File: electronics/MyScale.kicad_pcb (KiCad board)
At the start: 2 copper layers, 74 x 50 mm, 50 parts, among them J1 Conn_01x03, J2 Conn_01x03, J3 Conn_01x03, J4 Conn_01x03, J5 Conn_01x02_MountingPin, J6 12402012E212A, J7 Conn_01x03, Q1 DMG2305UX, Q4 PNP, SW1 SW_Push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

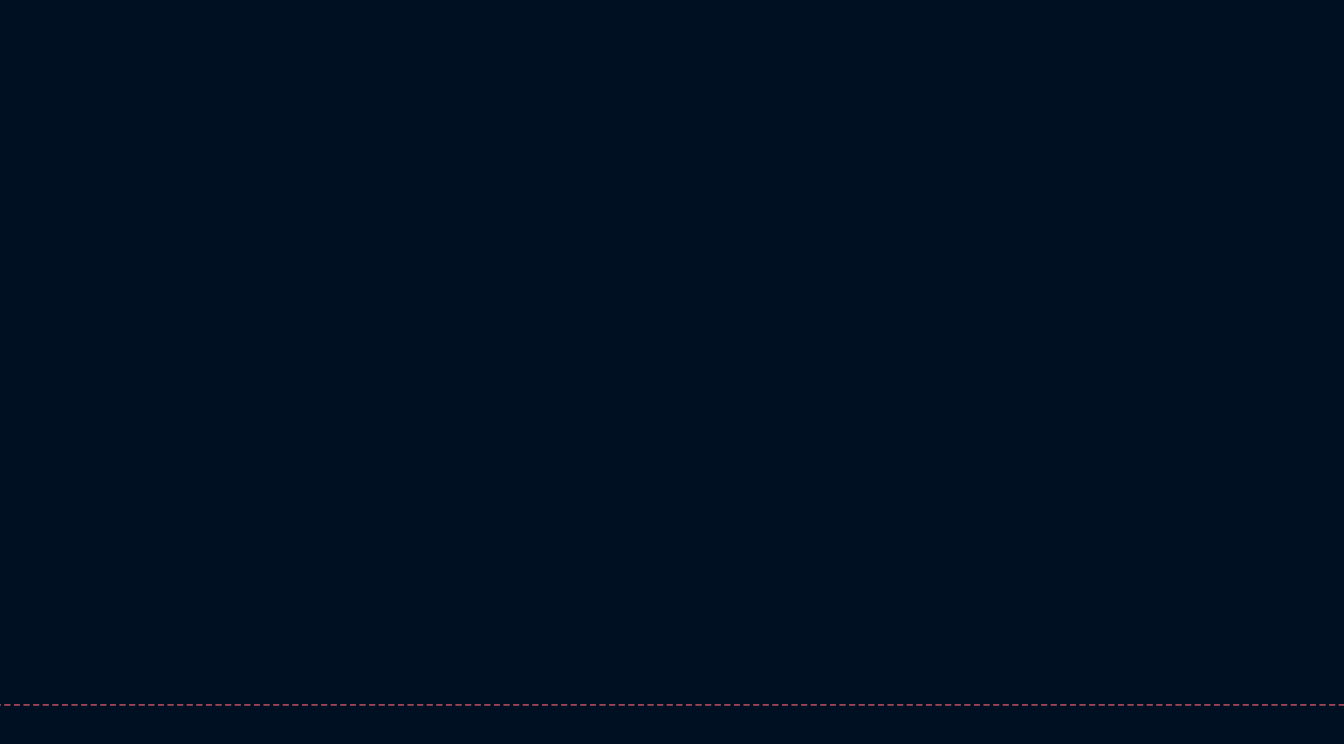
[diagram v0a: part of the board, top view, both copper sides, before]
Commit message: electronics: start with A7670 module
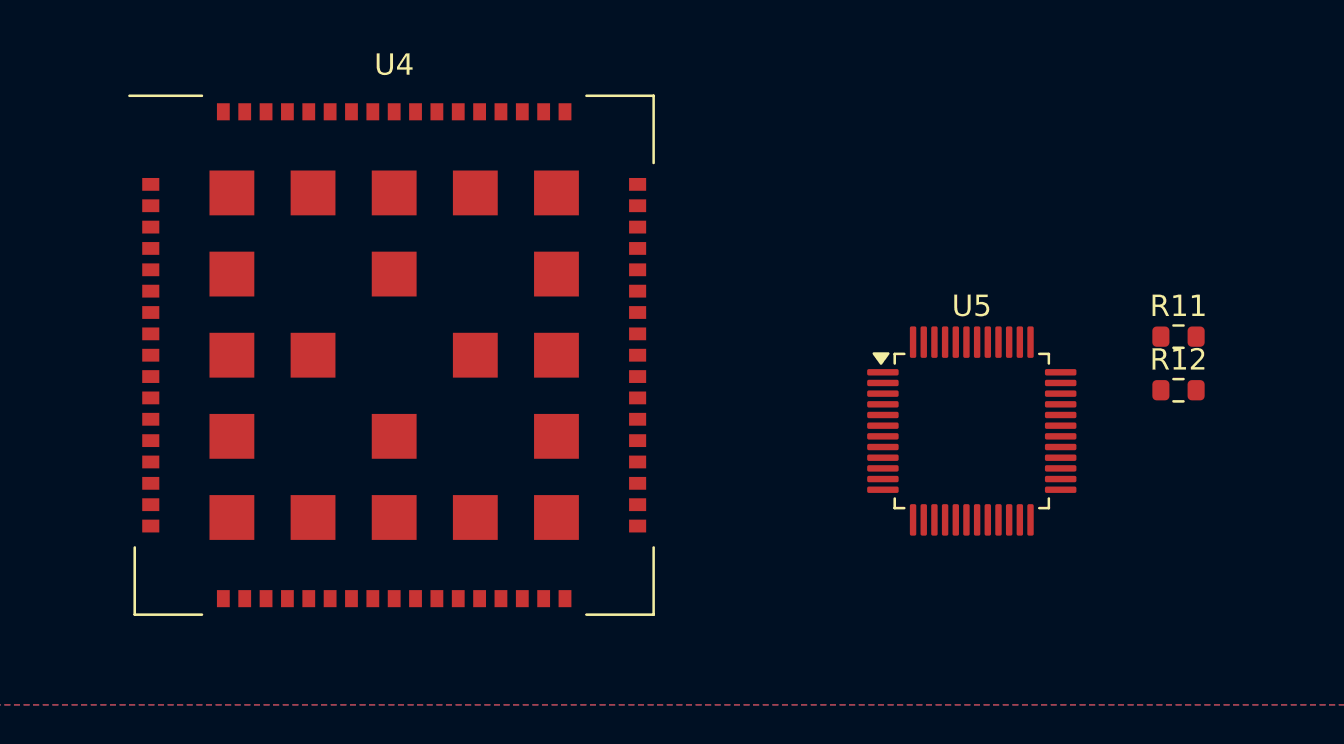
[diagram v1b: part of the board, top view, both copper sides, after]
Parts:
- added R11: 100k, Resistor_SMD:R_0603_1608Metric, F.Cu at (182.4, 17.8)
- added R12: 100k, Resistor_SMD:R_0603_1608Metric, F.Cu at (182.4, 20.3)
- added U4: ~, MyScale:A7670, F.Cu at (145.6, 18.6)
- added U5: STM32U083CCTx, Package_QFP:LQFP-48_7x7mm_P0.5mm, F.Cu at (172.7, 22.2)
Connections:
- R1 pad 1: Net-(U2-IO15) -> unconnected-(R1-Pad1)

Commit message: schematics
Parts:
- removed C3: 1u, Capacitor_SMD:C_0603_1608Metric
- removed C7: 10u, Capacitor_SMD:C_0603_1608Metric
- removed C8: 0.1u, Capacitor_SMD:C_0603_1608Metric
- removed J7: Conn_01x03, Connector_PinHeader_2.54mm:PinHeader_1x03_P2.54mm_Vertical
- removed R14, R15: 10k, Resistor_SMD:R_0603_1608Metric
- removed REF** (x3): Tab, MyScale:KikitTab
- removed SW1: SW_Push, Button_Switch_SMD:SW_SPST_TL3305A
- removed U3: AP2112K-3.3, Package_TO_SOT_SMD:SOT-23-5
- added C27: 1u, Capacitor_SMD:C_0402_1005Metric, F.Cu at (251.2, 45.0)
- added C28: 10n, Capacitor_SMD:C_0402_1005Metric, F.Cu at (251.2, 47.0)
- added C29: 0.1u, Capacitor_SMD:C_0402_1005Metric, F.Cu at (251.2, 48.9)
- added C30: 1u, Capacitor_SMD:C_0402_1005Metric, F.Cu at (251.2, 50.9)
- added C33: 0.1u, Capacitor_SMD:C_0603_1608Metric, F.Cu at (225.5, 76.1)
- added C34: 0.1u, Capacitor_SMD:C_0603_1608Metric, F.Cu at (225.5, 78.6)
- added C35: 1u, Capacitor_SMD:C_0603_1608Metric, F.Cu at (236.7, 80.7)
- added C36: 1u, Capacitor_SMD:C_0603_1608Metric, F.Cu at (225.5, 81.1)
- added C37: 1u, Capacitor_SMD:C_0603_1608Metric, F.Cu at (225.5, 83.6)
- added D5: LED, LED_SMD:LED_0603_1608Metric, F.Cu at (225.5, 71.5)
- added R17: 24k, Resistor_SMD:R_0402_1005Metric, F.Cu at (233.0, 71.2)
- added U6: TPS7A0518PDBV, Package_TO_SOT_SMD:SOT-23-5, F.Cu at (237.2, 77.2)
- added U7: TPS7A0533PDBV, Package_TO_SOT_SMD:SOT-23-5, F.Cu at (230.1, 77.2)
- C5: value 4.7u -> 1u
- R16: value 0R -> 51R
- U2: value ESP32-C6-WROOM-1-N8 -> TPS22953; footprint MyScale:MOD28_ESP32-C6-WROOM-1_EXP -> MyScale:TI_DQC0010A
- moved U2 122.7 mm to (251.7, 54.4), turned to 0 degrees
- moved R16 112.7 mm to (229.6, 71.5), turned to 0 degrees
- moved U4 98.8 mm to (236.6, 57.1)
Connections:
- C5 pad 1: +3V3 -> +1V8
- C6 pad 1: VBAT -> /Charger/Vpack
- D1 pad 2: +3V3 -> +1V8
- J5 pad 1: VBAT -> /Charger/Vpack
- Q1 pad 2: VBAT -> /Charger/Vpack
- R1 pad 1: unconnected-(R1-Pad1) -> /Led
- R11 pad 1: Net-(SW3-A) -> VBAT
- R16 pad 1: Net-(U2-3V3) -> GND
- R16 pad 2: +3V3 -> Net-(D5-K)
- R8 pad 1: Net-(SW3-A) -> VBAT
- SW3 pad 1: Net-(SW3-A) -> VBAT
- U1 pad 11: /Sck -> Net-(U1-PD_SCK)
- U1 pad 12: /Dout -> Net-(U1-DOUT)
- U2 pad 1: GND -> VBAT
- U2 pad 10: Net-(U2-IO8) -> VBAT
- U2 pad 11: unconnected-(U2-IO10-Pad11) -> GND
- U2 pad 2: Net-(U2-3V3) -> VBAT
- U2 pad 3: /Enable -> VBAT
- U2 pad 4: /Sck -> /Radio/Enable
- U2 pad 5: /Dout -> GND
- U2 pad 6: unconnected-(U2-IO6-Pad6) -> Net-(U2-CT)
- U2 pad 8: unconnected-(U2-IO0-Pad8) -> VBAT
- U2 pad 9: unconnected-(U2-IO1-Pad9) -> VBAT
- U33 pad 3: VBAT -> /Charger/Vpack
- U33 pad 4: VBAT -> /Charger/Vpack
- U4 pad 10: unconnected-(U4-RXD-Pad10) -> /Radio/UartRx
- U4 pad 27: unconnected-(U4-USB_DP-Pad27) -> /Radio/USBD+
- U4 pad 28: unconnected-(U4-USB_DN-Pad28) -> /Radio/USBD-
- U4 pad 30: unconnected-(U4-USIM_VDD-Pad30) -> /Radio/SimVcc
- U4 pad 31: unconnected-(U4-USIM_DATA-Pad31) -> /Radio/SimData
- U4 pad 32: unconnected-(U4-USIM_CLK-Pad32) -> /Radio/SimClk
- U4 pad 33: unconnected-(U4-USIM_RST-Pad33) -> /Radio/SimRst
- U4 pad 52: unconnected-(U4-NETLIGHT-Pad52) -> /Radio/LedNet
- U4 pad 60: unconnected-(U4-MAIN_ANT-Pad60) -> /Radio/RfAnt
- U4 pad 9: unconnected-(U4-TXD-Pad9) -> /Radio/UartTx
- U5 pad 1: +3.3V -> +1V8
- U5 pad 24: +3.3V -> +1V8
- U5 pad 48: +3.3V -> +1V8
- U5 pad 9: +3.3V -> +1V8
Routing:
- net (no net): track 0.00 -> 35.8 mm
- net /Charger/Vpack: track 0.00 -> 29.1 mm
- net Net-(U1-PD_SCK): track 0.00 -> 20.8 mm
- net /Sck: track 20.8 -> 0.00 mm
- net Net-(U1-DOUT): track 0.00 -> 20.1 mm
- net /Dout: track 20.1 -> 0.00 mm
- net Net-(SW3-A): track 16.9 -> 0.00 mm, vias 1 -> 0
- net VBAT: track 29.1 -> 16.9 mm, vias 0 -> 1
- net /GPIO9: track 10.6 -> 0.00 mm
- net Net-(U2-IO15): track 8.73 -> 0.00 mm
- net /Led: track 0.00 -> 8.73 mm
- net /UartTx: track 6.95 -> 0.00 mm
- net /UartRx: track 6.42 -> 0.00 mm
- net /Enable: track 5.18 -> 0.00 mm
- net Net-(U2-3V3): track 4.78 -> 0.00 mm
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
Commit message: electronics: select footprints
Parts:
- removed C2, C6: 4.7u, Capacitor_SMD:C_0603_1608Metric
- removed D3: RB521S30T1G, Diode_SMD:D_SOD-523
- removed Q1: DMG2305UX, Package_TO_SOT_SMD:SOT-23
- removed R7: 100k, Resistor_SMD:R_0603_1608Metric
- removed U33: MCP73831-2-MC, MyScale:MCP_73831-2-MC
- added C1: 4.7u, Capacitor_SMD:C_0603_1608Metric, F.Cu at (219.0, 123.2)
- added C10: 6.8p, Capacitor_SMD:C_0603_1608Metric, F.Cu at (219.0, 130.7)
- added C11: 0.1u, Capacitor_SMD:C_0603_1608Metric, F.Cu at (219.0, 133.2)
- added C17: 0.1u, Capacitor_SMD:C_0603_1608Metric, F.Cu at (223.0, 123.2)
- added C18: 10n, Capacitor_SMD:C_0603_1608Metric, F.Cu at (223.0, 125.7)
- added C19: 1u, Capacitor_SMD:C_0603_1608Metric, F.Cu at (223.0, 128.2)
- added C20: 0.1u, Capacitor_SMD:C_0603_1608Metric, F.Cu at (219.0, 97.3)
- added C21: 22p, Capacitor_SMD:C_0603_1608Metric, F.Cu at (219.0, 99.8)
- added C22: 22p, Capacitor_SMD:C_0603_1608Metric, F.Cu at (219.0, 102.3)
- added C23: 22p, Capacitor_SMD:C_0603_1608Metric, F.Cu at (219.0, 104.8)
- added C24: 10p, Capacitor_SMD:C_0603_1608Metric, F.Cu at (219.0, 107.3)
- added C25: 100u, Capacitor_SMD:C_1210_3225Metric, F.Cu at (238.9, 95.6)
- added C26: 100u, Capacitor_SMD:C_1210_3225Metric, F.Cu at (238.9, 99.9)
- added C3: C, Capacitor_SMD:C_0402_1005Metric, F.Cu at (232.9, 117.0)
- added C32: 100u, Capacitor_SMD:CP_Elec_6.3x7.7, F.Cu at (226.2, 114.0)
- added C38: 47n, Capacitor_SMD:C_0603_1608Metric, F.Cu at (248.4, 94.8)
- added C39: 10u, Capacitor_SMD:C_0805_2012Metric, F.Cu at (252.6, 99.9)
- added C4: 4.7u, Capacitor_SMD:C_0603_1608Metric, F.Cu at (219.0, 125.7)
- added C40: 2.2u, Capacitor_SMD:C_0603_1608Metric, F.Cu at (248.4, 97.3)
- added C41: 2.2u, Capacitor_SMD:C_0603_1608Metric, F.Cu at (248.4, 99.8)
- added C42: 2.2u, Capacitor_SMD:C_0603_1608Metric, F.Cu at (248.4, 102.3)
- added C7: C, Capacitor_SMD:C_0402_1005Metric, F.Cu at (232.9, 119.0)
- added C8: 33p, Capacitor_SMD:C_0603_1608Metric, F.Cu at (219.0, 94.8)
- added C9: 6.8p, Capacitor_SMD:C_0603_1608Metric, F.Cu at (219.0, 128.2)
- added J7: SIM_Card, Connector_Card:nanoSIM_Hinged_CUI_NSIM-2-C, F.Cu at (228.5, 101.9)
- added J9: Conn_Coaxial_Small, Connector_Coaxial:U.FL_Hirose_U.FL-R-SMT-1_Vertical, F.Cu at (239.1, 105.0)
- added R13: 22R, Resistor_SMD:R_0603_1608Metric, F.Cu at (219.0, 112.3)
- added R14: 22R, Resistor_SMD:R_0603_1608Metric, F.Cu at (219.0, 114.8)
- added R15: 0R, Resistor_SMD:R_0402_1005Metric, F.Cu at (242.9, 103.0)
- added R2: 10k, Resistor_SMD:R_0603_1608Metric, F.Cu at (223.0, 130.7)
- added R22: 10k, Resistor_SMD:R_0402_1005Metric, F.Cu at (242.9, 105.0)
- added R23: 0R, Resistor_SMD:R_0603_1608Metric, F.Cu at (248.4, 104.8)
- added R24: 10k, Resistor_SMD:R_0603_1608Metric, F.Cu at (248.4, 107.3)
- added R25: 10k, Resistor_SMD:R_0603_1608Metric, F.Cu at (248.4, 109.8)
- added R26: 10k, Resistor_SMD:R_0402_1005Metric, F.Cu at (242.9, 107.0)
- added R5: 0R, Resistor_SMD:R_0603_1608Metric, F.Cu at (223.0, 133.2)
- added R6: 22R, Resistor_SMD:R_0603_1608Metric, F.Cu at (219.0, 109.8)
- added SW1: SW_Push, Button_Switch_SMD:SW_SPST_TL3305A, F.Cu at (236.6, 113.0)
- added U3: ~, Package_SO:VSSOP-8_2.3x2mm_P0.5mm, F.Cu at (249.2, 115.0)
- added U8: BQ25302RTER, MyScale:TI_RTE0016C, F.Cu at (252.8, 95.9)
- added Y1: Crystal, Crystal:Crystal_SMD_2012-2Pin_2.0x1.2mm, F.Cu at (227.0, 132.9)
- R9: value 4.7k -> 20k
- U5: value STM32U083CCTx -> STM32U083CCUx; footprint Package_QFP:LQFP-48_7x7mm_P0.5mm -> Package_DFN_QFN:QFN-48-1EP_7x7mm_P0.5mm_EP5.6x5.6mm
- moved U5 119.1 mm to (230.1, 126.6)
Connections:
- net /Radio/Enable renamed /RadioEnable
- net /Radio/UartRx renamed /RadioUartTx
- net /Radio/UartTx renamed /RadioUartRx
- J6 pad A6: unconnected-(J6-D+-PadA6) -> /USBD+
- J6 pad A7: unconnected-(J6-D--PadA7) -> /USBD-
- J6 pad B6: unconnected-(J6-D+-PadB6) -> /USBD+
- J6 pad B7: unconnected-(J6-D--PadB7) -> /USBD-
- R11 pad 2: /Charger/VbatSense -> /VbatSense
- R12 pad 1: /Charger/VbatSense -> /VbatSense
- SW3 pad 2: Net-(D3-K) -> /Charger/Vpack
- U4 pad 1: unconnected-(U4-PWRKEY-Pad1) -> /Radio/PwrKey
- U4 pad 16: unconnected-(U4-RESET-Pad16) -> /Radio/Reset
- U4 pad 24: unconnected-(U4-VBUS-Pad24) -> VBUS
- U4 pad 27: /Radio/USBD+ -> /USBD+
- U4 pad 28: /Radio/USBD- -> /USBD-
- U5 pad 10: unconnected-(U5-PA0-Pad10) -> /VbatSense
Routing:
- net Net-(D3-K): track 10.6 -> 0.00 mm, vias 1 -> 0
- net /Charger/Vpack: track 29.1 -> 39.7 mm, vias 0 -> 1
- added copper zone on F.Cu, net /Charger/Vpack
- removed copper zone on F.Cu, net Net-(D3-K)

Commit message: electronics: initial placement
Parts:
- added D2: D_Schottky, Diode_SMD:D_SOD-523, F.Cu at (122.1, 152.3)
- added J10: Conn_02x03_Odd_Even, Connector:Tag-Connect_TC2030-IDC-NL_2x03_P1.27mm_Vertical, F.Cu at (120.1, 127.8)
- added L1: 1u, MyScale:MG_MAPM0420F, F.Cu at (129.1, 137.3)
- added Q1: Q_NMOS_GSD, Package_TO_SOT_SMD:SOT-23-3, F.Cu at (73.4, 127.9)
- C41: value 2.2u -> 10u; footprint Capacitor_SMD:C_0603_1608Metric -> Capacitor_SMD:C_0805_2012Metric
- R11: value 100k -> 20k
- R12: value 100k -> 10k
- moved R22 173.6 mm to (70.8, 127.4), turned to -90 degrees
- moved R26 172.6 mm to (74.7, 145.8)
- moved U4 169.3 mm to (88.3, 138.8)
- moved C27 167.8 mm to (106.3, 129.5), turned to 180 degrees
- moved SW1 165.0 mm to (73.0, 134.4), turned to 90 degrees
- moved C29 164.8 mm to (107.7, 130.0), turned to -90 degrees
- moved C28 161.6 mm to (109.7, 125.1), turned to 90 degrees
- moved C30 161.2 mm to (108.2, 125.5)
- moved U2 161.1 mm to (108.2, 127.5), turned to 90 degrees
- moved R15 156.1 mm to (88.1, 123.6), turned to 90 degrees
- moved J9 154.8 mm to (85.0, 119.6), turned to 90 degrees
- moved C20 153.2 mm to (78.0, 157.3)
- moved C21 153.2 mm to (78.0, 159.8)
- moved C22 153.2 mm to (78.0, 162.3)
- moved C23 153.2 mm to (78.0, 164.8)
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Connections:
- C24 pad 1: VBAT -> /Radio/VbatModule
- C25 pad 1: VBAT -> /Radio/VbatModule
- C26 pad 1: VBAT -> /Radio/VbatModule
- C30 pad 1: VBAT -> /Radio/VbatModule
- C32 pad 1: VBAT -> /Radio/VbatModule
- C38 pad 1: Net-(U8-SW) -> Net-(C38-Pad1)
- C8 pad 1: VBAT -> /Radio/VbatModule
- R26 pad 1: VBAT -> /Radio/VbatModule
- U2 pad 10: VBAT -> /Radio/VbatModule
- U2 pad 8: VBAT -> /Radio/VbatModule
- U2 pad 9: VBAT -> /Radio/VbatModule
- U3 pad 1: /Sck -> Net-(U1-PD_SCK)
- U3 pad 3: +3V3 -> +1V8
- U3 pad 4: Net-(U1-PD_SCK) -> /Sck
- U3 pad 5: Net-(U1-DOUT) -> /Dout
- U3 pad 7: +1V8 -> +3V3
- U3 pad 8: /Dout -> Net-(U1-DOUT)
- U4 pad 55: VBAT -> /Radio/VbatModule
- U4 pad 56: VBAT -> /Radio/VbatModule
- U4 pad 57: VBAT -> /Radio/VbatModule
- U8 pad 1: /Charger/REGN -> VBUS
- U8 pad 10: Net-(U8-TS) -> /Charger/Vpack
- U8 pad 13: Net-(U8-SW) -> Net-(C38-Pad1)
- U8 pad 14: Net-(U8-BTST) -> Net-(C38-Pad1)
- U8 pad 15: Net-(U8-PMID) -> Net-(U8-BTST)
- U8 pad 16: VBUS -> Net-(U8-PMID)
- U8 pad 2: Net-(U8-ICHG_EN) -> /Charger/REGN
- U8 pad 4: Net-(U8-VSET) -> Net-(U8-ICHG_EN)
- U8 pad 5: Net-(U8-NC-Pad5) -> Net-(U8-NC)
- U8 pad 6: /Charger/Vpack -> unconnected-(U8-~{EN}-Pad6)
- U8 pad 7: Net-(U8-NC-Pad5) -> Net-(U8-TS)
- U8 pad 8: Net-(U8-NC-Pad5) -> Net-(U8-NC)
- U8 pad 9: Net-(U8-NC-Pad5) -> Net-(U8-VSET)
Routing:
- net +3V3: track 94.3 -> 6.99 mm, vias 2 -> 0
- net (no net): track 35.8 -> 0.00 mm
- net /Charger/Vpack: track 39.7 -> 5.25 mm, vias 1 -> 0
- net /Load Cell Interface/A+: track 28.8 -> 6.85 mm
- net Net-(U1-PD_SCK): track 20.8 -> 4.84 mm
- net /Load Cell Interface/E+: track 23.6 -> 7.87 mm
- net Net-(U1-DOUT): track 20.1 -> 4.98 mm
- net /Load Cell Interface/A-: track 15.3 -> 2.13 mm, vias 4 -> 2
- net VBUS: track 31.4 -> 19.4 mm
- net VBAT: track 16.9 -> 5.33 mm
- net /Led: track 8.73 -> 0.00 mm
- net Net-(U8-STAT): track 5.38 -> 0.00 mm, vias 2 -> 0
- net Net-(D4-K): track 5.39 -> 3.52 mm
- net Net-(U6-EN): track 1.76 -> 0.00 mm
- net Net-(U8-ICHG_EN): track 1.59 -> 0.00 mm
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- removed copper zone on F.Cu, net /Charger/Vpack
- removed copper zone on B.Cu, net GND
- removed copper zone on F.Cu, net GND
- removed copper zone on F.Cu, net VBAT
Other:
- board size 74 x 50 mm -> 90 x 70 mm
- board text added: "DCEIQ r2"
- board text removed: "DCEIQ r1"

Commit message: electronics: start routing
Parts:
- added C43: 0.1u, Capacitor_SMD:C_0603_1608Metric, F.Cu at (104.5, 141.6)
- added R7: 10k, Resistor_SMD:R_0603_1608Metric, F.Cu at (106.1, 141.6)
- SW3: moved to F.Cu
- moved H3 147.8 mm to (65.2, 175.6)
- moved H1 112.2 mm to (138.8, 154.9)
- moved H2 62.5 mm to (65.6, 119.0)
- moved R8 35.1 mm to (125.5, 122.7), turned to -90 degrees
- moved C35 33.2 mm to (128.2, 121.7), turned to 180 degrees
- moved U6 30.6 mm to (128.0, 124.6), turned to -90 degrees
- moved C5 27.6 mm to (130.6, 125.0), turned to 90 degrees
- moved J5 26.7 mm to (140.7, 129.2)
- moved SW3 20.5 mm to (143.3, 119.7), turned to 90 degrees
- moved C40 11.8 mm to (132.5, 143.3), turned to -90 degrees
- moved R17 11.6 mm to (111.9, 118.2), turned to 90 degrees
- moved C29 10.7 mm to (112.9, 120.6)
- moved C27 10.6 mm to (111.9, 120.6), turned to -90 degrees
- moved R24 9.94 mm to (128.6, 136.5), turned to 180 degrees
- moved C41 9.79 mm to (130.7, 144.5), turned to -90 degrees
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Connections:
- SW3 pad 1: VBAT -> unconnected-(SW3-A-Pad1)
- SW3 pad 3: unconnected-(SW3-C-Pad3) -> VBAT
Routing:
- net /Charger/Vpack: track 5.25 -> 45.0 mm
- net VBAT: track 5.33 -> 29.1 mm, vias 1 -> 0
- net /Radio/VbatModule: track 0.00 -> 12.6 mm
- net /Load Cell Interface/A+: track 6.85 -> 18.7 mm
- net /Load Cell Interface/E+: track 7.87 -> 18.2 mm
- net +1V8: track 0.00 -> 9.54 mm
- net /Load Cell Interface/A-: track 2.13 -> 7.43 mm
- net /~{Reset}: track 0.00 -> 5.02 mm
- net Net-(U5-PC15): track 0.00 -> 4.06 mm
- net Net-(U5-PC14): track 0.00 -> 3.97 mm
- net Net-(D4-K): track 3.52 -> 0.00 mm
- net +3V3: track 6.99 -> 3.60 mm
- net Net-(U8-TS): track 0.00 -> 2.91 mm
- net /Radio/LedNet: track 0.00 -> 2.71 mm
- net Net-(J6-CC2): track 1.62 -> 4.11 mm
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- added copper zone on F.Cu, net /Charger/Vpack
- added copper zone on F.Cu, net /Radio/VbatModule
- added copper zone on F.Cu, net Net-(C38-Pad1)
- added copper zone on F.Cu, net VBAT
- added copper zone on F.Cu, net VBUS
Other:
- board size 90 x 70 mm -> 83.5 x 64.7 mm
- copper layers 2 -> 4

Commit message: electronics: more routing
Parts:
- moved D2 25.5 mm to (106.5, 132.2)
- moved R11 25.5 mm to (106.6, 129.1)
- moved R12 25.5 mm to (106.6, 130.6)
- moved R14 19.7 mm to (90.2, 159.3), turned to 180 degrees
- moved C5 16.3 mm to (114.9, 129.7)
- moved R8 16.3 mm to (109.9, 127.3)
- moved C35 16.3 mm to (112.6, 126.4)
- moved U6 16.3 mm to (112.4, 129.3)
- moved R13 16.1 mm to (90.1, 161.7), turned to 180 degrees
- moved C23 15.0 mm to (90.9, 157.1), turned to 90 degrees
- moved C22 14.5 mm to (92.4, 163.9), turned to -90 degrees
- moved C21 14.4 mm to (92.4, 160.8), turned to 90 degrees
- moved R6 13.8 mm to (90.1, 163.2), turned to 180 degrees
- moved C20 11.4 mm to (89.4, 157.1), turned to -90 degrees
- moved J7 7.24 mm to (80.7, 159.7), turned to -90 degrees
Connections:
- U8 pad 5: Net-(U8-NC) -> unconnected-(U8-POL-Pad5)
- U8 pad 8: Net-(U8-NC) -> unconnected-(U8-NC-Pad8)
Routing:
- net /Radio/SimData: track 0.00 -> 15.8 mm, vias 0 -> 2
- net /Radio/SimClk: track 0.00 -> 14.2 mm, vias 0 -> 2
- net /Radio/SimRst: track 0.00 -> 12.8 mm
- net /Radio/SimVcc: track 0.00 -> 9.42 mm
- net /Charger/REGN: track 1.32 -> 5.83 mm, vias 0 -> 2
- net Net-(J7-RST): track 0.00 -> 1.96 mm
- net Net-(J7-I/O): track 0.00 -> 1.92 mm
- net Net-(J7-CLK): track 0.00 -> 1.83 mm
- net GND: vias 1 -> 0

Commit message: electronics: sync
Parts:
- moved J9 3.37 mm to (88.3, 119.0)
- moved C3 0.20 mm to (87.8, 125.2)
- moved C7 0.20 mm to (87.8, 122.1)
- moved R15 0.20 mm to (88.3, 123.6)
- turned J10 to 180 degrees
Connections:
- J10 pad 6: /SWDCLK -> /SWCLK
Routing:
- net VBAT: track 29.1 -> 48.4 mm
- net /Radio/PwrKey: track 0.00 -> 12.5 mm
- net /SWCLK: track 0.00 -> 9.13 mm
- net /VbatSense: track 0.00 -> 3.11 mm
- net /Radio/Reset: track 0.00 -> 1.74 mm
- net +3V3: track 3.60 -> 5.31 mm
- net /CellsEnable: track 0.00 -> 1.64 mm
- net +1V8: track 9.54 -> 11.1 mm
- net Net-(U6-EN): track 0.00 -> 1.57 mm
- net /RadioPwrKey: track 0.00 -> 1.48 mm
- added copper zone on B.Cu, net GND
- added copper zone on F.Cu, net GND
- added copper zone on In1.Cu, net GND
